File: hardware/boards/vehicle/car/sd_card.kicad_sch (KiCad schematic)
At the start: 4 parts

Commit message: added all footprints for lidar and car
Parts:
- C17, C18: footprint (none) -> Capacitor_SMD:C_0603_1608Metric_Pad1.08x0.95mm_HandSolder
- R99: footprint (none) -> Resistor_SMD:R_0603_1608Metric_Pad0.98x0.95mm_HandSolder
- SD1: footprint (none) -> air_sens_foots:SD_SLOT
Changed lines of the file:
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@@
 			)
 		)
-		(property "Footprint" ""
+		(property "Footprint" "Capacitor_SMD:C_0603_1608Metric_Pad1.08x0.95mm_HandSolder"
 			(at 160.9852 93.98 0)
 			(effects
@@
 			)
 		)
-		(property "Footprint" ""
+		(property "Footprint" "Resistor_SMD:R_0603_1608Metric_Pad0.98x0.95mm_HandSolder"
 			(at 117.602 83.82 90)
 			(effects
@@
 			)
 		)
-		(property "Footprint" ""
+		(property "Footprint" "Capacitor_SMD:C_0603_1608Metric_Pad1.08x0.95mm_HandSolder"
 			(at 172.4152 93.98 0)
 			(effects
@@
 			)
 		)
-		(property "Footprint" ""
+		(property "Footprint" "air_sens_foots:SD_SLOT"
 			(at 142.24 90.17 0)
 			(effects

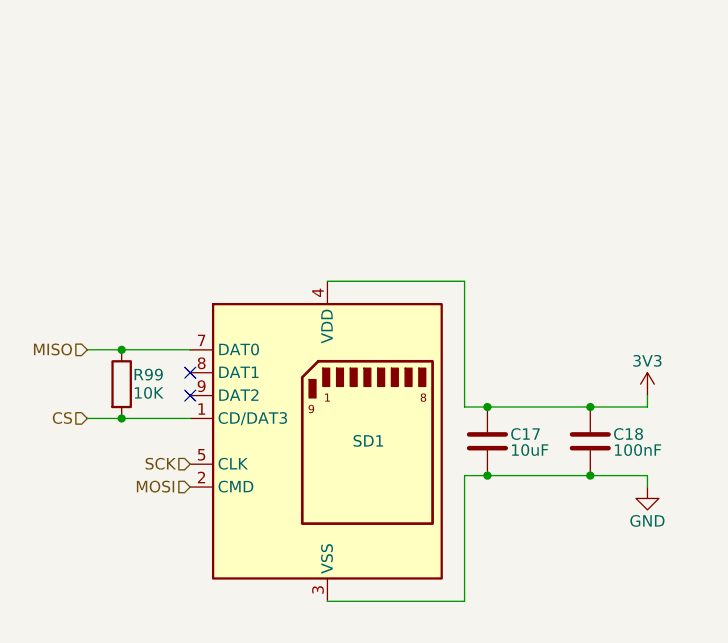
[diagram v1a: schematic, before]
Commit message: corrected SD card and transceiver on symbol and schema
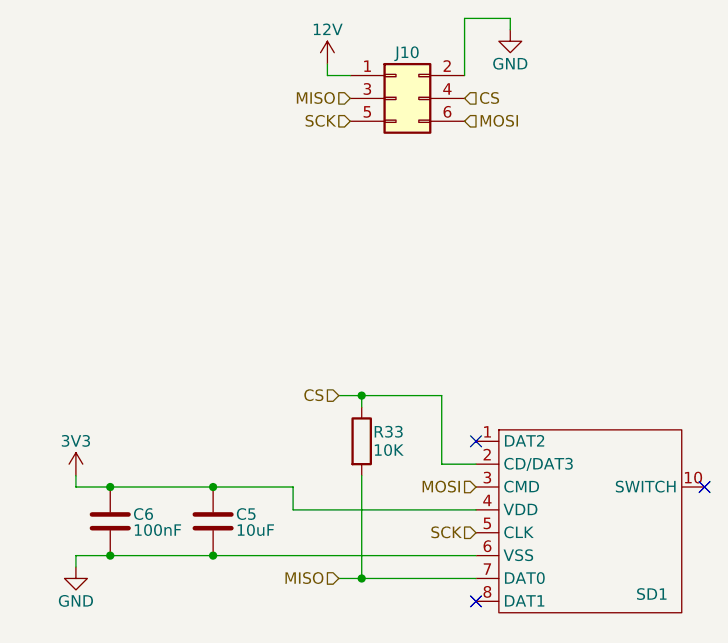
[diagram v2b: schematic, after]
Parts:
- removed C17: 10uF, Capacitor_SMD:C_0603_1608Metric_Pad1.08x0.95mm_HandSolder, symbol Device:C
- removed C18: 100nF, Capacitor_SMD:C_0603_1608Metric_Pad1.08x0.95mm_HandSolder, symbol Device:C
- removed R99: 10K, Resistor_SMD:R_0603_1608Metric_Pad0.98x0.95mm_HandSolder, symbol Device:R
- removed SD1: SD_Card_Device, air_sens_foots:SD_SLOT, symbol Connector:SD_Card_Device
- added C5: 10uF, Capacitor_SMD:C_0603_1608Metric_Pad1.08x0.95mm_HandSolder, symbol Device:C
- added C6: 100nF, Capacitor_SMD:C_0603_1608Metric_Pad1.08x0.95mm_HandSolder, symbol Device:C
- added J10: Conn_02x03_Odd_Even, Connector_PinHeader_2.54mm:PinHeader_2x03_P2.54mm_Vertical, symbol Connector_Generic:Conn_02x03_Odd_Even
- added R33: 10K, Resistor_SMD:R_0603_1608Metric_Pad0.98x0.95mm_HandSolder, symbol Device:R
- added SD1: ~, air_sens_foots:SD_SLOT, symbol air_sens_lib:SD_SLOT
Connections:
- net 3V3: now also C5.1, C6.1, SD1.4 (VDD)
- net CS: now also J10.4 (Pin_4), R33.1, SD1.2 (CD/DAT3)
- net GND: now also C5.2, C6.2, J10.2 (Pin_2), SD1.6 (VSS)
- net MISO: now also J10.3 (Pin_3), R33.2, SD1.7 (DAT0)
- net MOSI: now also J10.6 (Pin_6), SD1.3 (CMD)
- net SCK: now also J10.5 (Pin_5), SD1.5 (CLK)
- new net 12V: J10.1 (Pin_1)
- no-connect marks 2 -> 3

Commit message: pcb for car
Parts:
- removed R33: 10K, Resistor_SMD:R_0603_1608Metric_Pad0.98x0.95mm_HandSolder, symbol Device:R
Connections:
- net 12V is gone; now on net CS: J10.1 (Pin_1)
- net 3V3: now also J10.4 (Pin_4)
- net CS: no longer J10.4 (Pin_4)
- net GND: now also J10.6 (Pin_6); no longer J10.2 (Pin_2)
- net MISO: now also J10.5 (Pin_5); no longer J10.3 (Pin_3)
- net MOSI: now also J10.2 (Pin_2); no longer J10.6 (Pin_6)
- net SCK: now also J10.3 (Pin_3); no longer J10.5 (Pin_5)
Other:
- moved on the sheet: C5, C6
